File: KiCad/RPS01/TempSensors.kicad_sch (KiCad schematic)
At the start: 4 parts, among them J7 JST_PH_TEMP_SENSOR_1, J7 JST_PH_TEMP_SENSOR_2, J7 JST_PH_TEMP_SENSOR_3

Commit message: Large Schematic Update
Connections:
- net Temperature Data renamed VSIG
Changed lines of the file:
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@@
   (junction (at 139.1158 78.74) (diameter 0) (color 0 0 0 0)
   )
-  (junction (at 139.1158 78.8097) (diameter 0) (color 0 0 0 0)
+  (junction (at 146.7358 93.5482) (diameter 0) (color 0 0 0 0)
   )
-  (junction (at 146.7358 93.5482) (diameter 0) (color 0 0 0 0)
+  (junction (at 139.1158 79.502) (diameter 0) (color 0 0 0 0)
   )
   (junction (at 125.73 91.0082) (diameter 0) (color 0 0 0 0)
@@
   (junction (at 146.7358 106.7054) (diameter 0) (color 0 0 0 0)
   )
-  (wire (pts (xy 139.1158 78.8097) (xy 139.1158 91.0082))
+  (wire (pts (xy 125.73 91.0082) (xy 125.73 104.394))
     (stroke (width 0) (type default))
   )
-  (wire (pts (xy 125.73 91.0082) (xy 125.73 104.394))
+  (wire (pts (xy 125.73 90.17) (xy 125.73 91.0082))
     (stroke (width 0) (type default))
   )
@@
     (stroke (width 0) (type default))
   )
-  (wire (pts (xy 125.73 78.8097) (xy 125.73 90.17))
+  (wire (pts (xy 125.73 79.502) (xy 125.73 90.17))
     (stroke (width 0) (type default))
   )
@@
     (stroke (width 0) (type default))
   )
-  (wire (pts (xy 139.1158 78.8097) (xy 125.73 78.8097))
+  (wire (pts (xy 139.1158 79.502) (xy 125.73 79.502))
     (stroke (width 0) (type default))
   )
@@
     (stroke (width 0) (type default))
   )
-  (wire (pts (xy 125.73 90.17) (xy 125.73 91.0082))
-    (stroke (width 0) (type default))
-  )
   (wire (pts (xy 137.3886 75.7682) (xy 148.2598 75.7682))
     (stroke (width 0) (type default))
@@
     (stroke (width 0) (type default))
   )
-  (wire (pts (xy 125.73 78.74) (xy 139.1158 78.74))
+  (wire (pts (xy 139.1158 79.502) (xy 139.1158 91.0082))
     (stroke (width 0) (type default))
   )
@@
     (stroke (width 0) (type default))
   )
-  (wire (pts (xy 139.1158 78.74) (xy 139.1158 78.8097))
+  (wire (pts (xy 139.1158 78.74) (xy 139.1158 79.502))
     (stroke (width 0) (type default))
   )
@@
     (stroke (width 0) (type default))
   )
-  (hierarchical_label "Temperature Data" (shape input) (at 111.76 90.17 180) (fields_autoplaced)
+  (hierarchical_label "VSIG" (shape input) (at 111.76 90.17 180) (fields_autoplaced)
     (effects (font (size 1.27 1.27)) (justify right))
   )

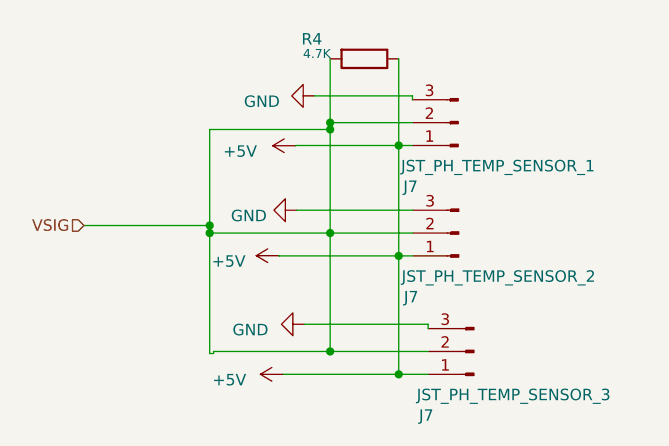
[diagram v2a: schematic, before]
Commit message: Finished most of the Schematics. Needs polishing
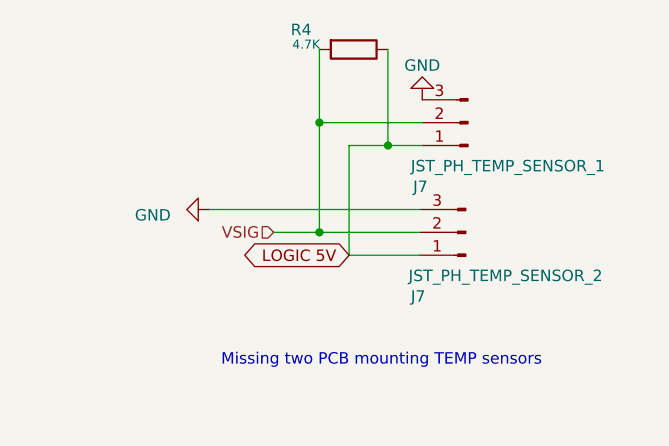
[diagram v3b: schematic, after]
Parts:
- removed J7: JST_PH_TEMP_SENSOR_3, Connector_JST:JST_PH_B3B-PH-K_1x03_P2.00mm_Vertical, symbol Connector:Conn_01x03_Pin
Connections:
- net +5V renamed LOGIC 5V
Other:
- note added: "Missing two PCB mounting TEMP sensors"
- moved on the sheet: J7, R4

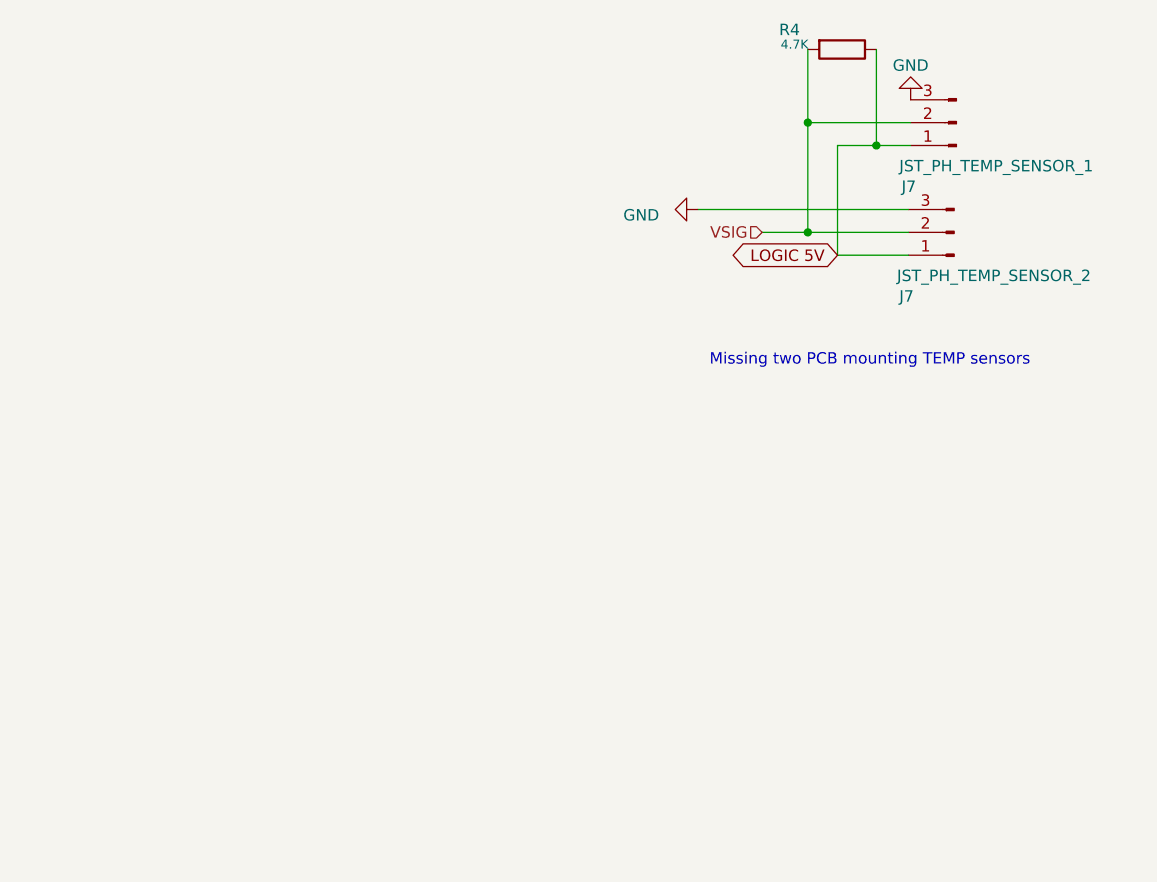
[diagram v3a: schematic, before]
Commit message: Finished Updating Footprints and Reorganized Reference Designators
Finished Updating Footprints and Reorganized Reference Designators

Starting to work on Final PCB, except for 19V Boost. Please check Schematic for errors
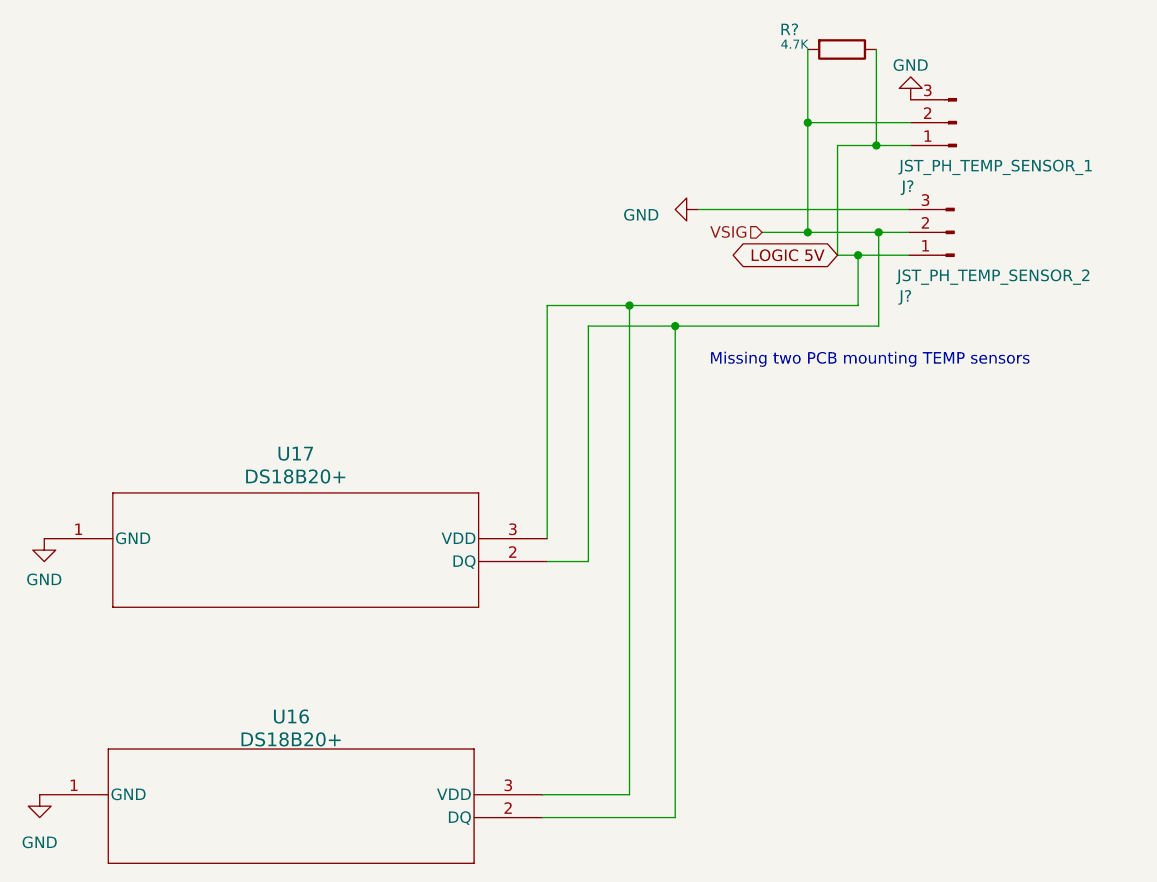
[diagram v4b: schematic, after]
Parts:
- added U16, U17: DS18B20+, Mechatronics TEMP:21-0248A_Q3-1_MXM, symbol Mechatronics TEMP:DS18B20+
- renumbered J7 to J?, R4 to R?
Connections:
- net GND: now also U16.1 (GND), U17.1 (GND)
- net LOGIC 5V: now also U16.3 (VDD), U17.3 (VDD)
- net VSIG: now also U16.2 (DQ), U17.2 (DQ)
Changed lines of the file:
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@@
 (kicad_sch (version 20230121) (generator eeschema)
   (paper "A4")
+  (junction (at 118.11 99.06) (diameter 0) (color 0 0 0 0)
+  )
   (junction (at 137.922 78.74) (diameter 0) (color 0 0 0 0)
   )
@@
   (junction (at 145.542 81.28) (diameter 0) (color 0 0 0 0)
   )
+  (junction (at 143.51 93.472) (diameter 0) (color 0 0 0 0)
+  )
+  (junction (at 145.796 90.932) (diameter 0) (color 0 0 0 0)
+  )
+  (junction (at 123.19 101.346) (diameter 0) (color 0 0 0 0)
+  )
   (wire (pts (xy 132.842 90.932) (xy 137.922 90.932))
     (stroke (width 0) (type default))
   )
+  (wire (pts (xy 143.51 99.06) (xy 143.51 93.472))
+    (stroke (width 0) (type default))
+  )
+  (wire (pts (xy 145.796 90.932) (xy 137.922 90.932))
+    (stroke (width 0) (type default))
+  )
+  (wire (pts (xy 108.966 127.508) (xy 113.538 127.508))
+    (stroke (width 0) (type default))
+  )
+  (wire (pts (xy 118.11 99.06) (xy 143.51 99.06))
+    (stroke (width 0) (type default))
+  )
+  (wire (pts (xy 108.458 153.416) (xy 118.11 153.416))
+    (stroke (width 0) (type default))
+  )
   (wire (pts (xy 141.224 81.28) (xy 141.224 93.472))
     (stroke (width 0) (type default))
   )
-  (wire (pts (xy 149.098 90.932) (xy 137.922 90.932))
+  (wire (pts (xy 149.098 90.932) (xy 145.796 90.932))
+    (stroke (width 0) (type default))
+  )
+  (wire (pts (xy 143.51 93.472) (xy 149.098 93.472))
     (stroke (width 0) (type default))
   )
@@
     (stroke (width 0) (type default))
   )
+  (wire (pts (xy 108.966 99.06) (xy 118.11 99.06))
+    (stroke (width 0) (type default))
+  )
+  (wire (pts (xy 113.538 101.346) (xy 123.19 101.346))
+    (stroke (width 0) (type default))
+  )
   (wire (pts (xy 137.922 70.612) (xy 137.922 78.74))
     (stroke (width 0) (type default))
   )
+  (wire (pts (xy 113.538 127.508) (xy 113.538 101.346))
+    (stroke (width 0) (type default))
+  )
+  (wire (pts (xy 118.11 153.416) (xy 118.11 99.06))
+    (stroke (width 0) (type default))
+  )
   (wire (pts (xy 137.922 78.74) (xy 149.352 78.74))
     (stroke (width 0) (type default))
@@
     (stroke (width 0) (type default))
   )
-  (wire (pts (xy 141.224 93.472) (xy 149.098 93.472))
+  (wire (pts (xy 141.224 93.472) (xy 143.51 93.472))
+    (stroke (width 0) (type default))
+  )
+  (wire (pts (xy 123.19 101.346) (xy 145.796 101.346))
     (stroke (width 0) (type default))
   )
@@
     (stroke (width 0) (type default))
   )
+  (wire (pts (xy 123.19 155.956) (xy 123.19 101.346))
+    (stroke (width 0) (type default))
+  )
+  (wire (pts (xy 108.966 124.968) (xy 108.966 99.06))
+    (stroke (width 0) (type default))
+  )
   (wire (pts (xy 145.542 81.28) (xy 149.352 81.28))
+    (stroke (width 0) (type default))
+  )
+  (wire (pts (xy 108.458 155.956) (xy 123.19 155.956))
+    (stroke (width 0) (type default))
+  )
+  (wire (pts (xy 145.796 101.346) (xy 145.796 90.932))
     (stroke (width 0) (type default))
   )
@@
   (symbol (lib_id "Device:R") (at 141.732 70.612 270) (unit 1)
     (in_bom yes) (on_board yes) (dnp no)
-    (property "Reference" "R4" (at 135.89 68.4276 90)
+    (property "Reference" "R?" (at 135.89 68.4276 90)
       (effects (font (size 1.27 1.27)))
     )
@@
       (project "MCU2"
         (path "/049009a7-95d1-4ccf-a10c-7859cfd6b188"
-          (reference "R4") (unit 1)
+          (reference "R?") (unit 1)
         )
       )
       (project "rps01"
         (path "/14930f15-c0a0-4b55-93e6-b112548415f6/a2e49fe6-126d-427d-b045-54fb7f662aa7"
-          (reference "R7") (unit 1)
+          (reference "R?") (unit 1)
         )
         (path "/14930f15-c0a0-4b55-93e6-b112548415f6"
-          (reference "R2") (unit 1)
-        )
-        (path "/14930f15-c0a0-4b55-93e6-b112548415f6/70788b2e-4f8b-415f-94db-6db5f6e45c82"
-          (reference "R19") (unit 1)
+          (reference "R?") (unit 1)
+        )
+        (path "/14930f15-c0a0-4b55-93e6-b112548415f6/70788b2e-4f8b-415f-94db-6db5f6e45c82"
+          (reference "R24") (unit 1)
         )
       )
       (project "M_MUC"
         (path "/8f0e16c9-4bd2-4a25-a569-54925ece9d23"
-          (reference "R1") (unit 1)
+          (reference "R?") (unit 1)
         )
       )
@@
   (symbol (lib_id "Connector:Conn_01x03_Pin") (at 154.178 90.932 180) (unit 1)
     (in_bom yes) (on_board yes) (dnp no)
-    (property "Reference" "J7" (at 148.082 98.044 0)
+    (property "Reference" "J?" (at 148.082 98.044 0)
       (effects (font (size 1.27 1.27)) (justify right))
     )
@@
       (project "rps01"
         (path "/14930f15-c0a0-4b55-93e6-b112548415f6/a2e49fe6-126d-427d-b045-54fb7f662aa7"
-          (reference "J7") (unit 1)
+          (reference "J?") (unit 1)
         )
         (path "/14930f15-c0a0-4b55-93e6-b112548415f6"
-          (reference "J11") (unit 1)
+          (reference "J?") (unit 1)
         )
         (path "/14930f15-c0a0-4b55-93e6-b112548415f6/70788b2e-4f8b-415f-94db-6db5f6e45c82"
@@
     )
   )
+  (symbol (lib_id "power:GND") (at 53.086 124.968 0) (unit 1)
+    (in_bom yes) (on_board yes) (dnp no) (fields_autoplaced)
+    (property "Reference" "#PWR044" (at 53.086 131.318 0)
+      (effects (font (size 1.27 1.27)) hide)
+    )
+    (property "Value" "GND" (at 53.086 129.54 0)
+      (effects (font (size 1.27 1.27)))
+    )
+    (property "Footprint" "" (at 53.086 124.968 0)
+      (effects (font (size 1.27 1.27)) hide)
+    )
+    (property "Datasheet" "" (at 53.086 124.968 0)
+      (effects (font (size 1.27 1.27)) hide)
+    )
+    (pin "1")
+    (instances
+      (project "rps01"
+        (path "/14930f15-c0a0-4b55-93e6-b112548415f6/70788b2e-4f8b-415f-94db-6db5f6e45c82"
+          (reference "#PWR044") (unit 1)
+        )
+      )
+    )
+  )
   (symbol (lib_id "power:GND") (at 149.352 76.2 180) (unit 1)
     (in_bom yes) (on_board yes) (dnp no) (fields_autoplaced)
-    (property "Reference" "#PWR044" (at 149.352 69.85 0)
+    (property "Reference" "#PWR046" (at 149.352 69.85 0)
       (effects (font (size 1.27 1.27)) hide)
     )
@@
       (project "rps01"
         (path "/14930f15-c0a0-4b55-93e6-b112548415f6/70788b2e-4f8b-415f-94db-6db5f6e45c82"
-          (reference "#PWR044") (unit 1)
+          (reference "#PWR046") (unit 1)
         )
       )
@@
   (symbol (lib_id "power:GND") (at 125.73 88.392 270) (unit 1)
     (in_bom yes) (on_board yes) (dnp no) (fields_autoplaced)
-    (property "Reference" "#PWR043" (at 119.38 88.392 0)
+    (property "Reference" "#PWR045" (at 119.38 88.392 0)
       (effects (font (size 1.27 1.27)) hide)
     )
@@
       (project "rps01"
         (path "/14930f15-c0a0-4b55-93e6-b112548415f6/70788b2e-4f8b-415f-94db-6db5f6e45c82"
+          (reference "#PWR045") (unit 1)
+        )
+      )
+    )
+  )
+  (symbol (lib_id "Mechatronics TEMP:DS18B20+") (at 52.578 153.416 0) (unit 1)
+    (in_bom yes) (on_board yes) (dnp no) (fields_autoplaced)
+    (property "Reference" "U16" (at 80.518 144.78 0)
+      (effects (font (size 1.524 1.524)))
+    )
+    (property "Value" "DS18B20+" (at 80.518 147.32 0)
+      (effects (font (size 1.524 1.524)))
+    )
+    (property "Footprint" "Mechatronics TEMP:21-0248A_Q3-1_MXM" (at 52.578 153.416 0)
+      (effects (font (size 1.27 1.27) italic) hide)
+    )
+    (property "Datasheet" "DS18B20+" (at 52.578 153.416 0)
+      (effects (font (size 1.27 1.27) italic) hide)
+    )
+    (pin "1")
+    (pin "2")
+    (pin "3")
+    (instances
+      (project "rps01"
+        (path "/14930f15-c0a0-4b55-93e6-b112548415f6/70788b2e-4f8b-415f-94db-6db5f6e45c82"
+          (reference "U16") (unit 1)
+        )
+      )
+    )
+  )
+  (symbol (lib_id "power:GND") (at 52.578 153.416 0) (unit 1)
+    (in_bom yes) (on_board yes) (dnp no) (fields_autoplaced)
+    (property "Reference" "#PWR043" (at 52.578 159.766 0)
+      (effects (font (size 1.27 1.27)) hide)
+    )
+    (property "Value" "GND" (at 52.578 158.75 0)
+      (effects (font (size 1.27 1.27)))
+    )
+    (property "Footprint" "" (at 52.578 153.416 0)
+      (effects (font (size 1.27 1.27)) hide)
+    )
+    (property "Datasheet" "" (at 52.578 153.416 0)
+      (effects (font (size 1.27 1.27)) hide)
+    )
+    (pin "1")
+    (instances
+      (project "rps01"
+        (path "/14930f15-c0a0-4b55-93e6-b112548415f6/70788b2e-4f8b-415f-94db-6db5f6e45c82"
           (reference "#PWR043") (unit 1)
+        )
+      )
+    )
+  )
+  (symbol (lib_id "Mechatronics TEMP:DS18B20+") (at 53.086 124.968 0) (unit 1)
+    (in_bom yes) (on_board yes) (dnp no) (fields_autoplaced)
+    (property "Reference" "U17" (at 81.026 115.57 0)
+      (effects (font (size 1.524 1.524)))
+    )
+    (property "Value" "DS18B20+" (at 81.026 118.11 0)
+      (effects (font (size 1.524 1.524)))
+    )
+    (property "Footprint" "Mechatronics TEMP:21-0248A_Q3-1_MXM" (at 53.086 124.968 0)
+      (effects (font (size 1.27 1.27) italic) hide)
+    )
+    (property "Datasheet" "DS18B20+" (at 53.086 124.968 0)
+      (effects (font (size 1.27 1.27) italic) hide)
+    )
+    (pin "1")
+    (pin "2")
+    (pin "3")
+    (instances
+      (project "rps01"
+        (path "/14930f15-c0a0-4b55-93e6-b112548415f6/70788b2e-4f8b-415f-94db-6db5f6e45c82"
+          (reference "U17") (unit 1)
         )
       )
@@
   (symbol (lib_id "Connector:Conn_01x03_Pin") (at 154.432 78.74 180) (unit 1)
     (in_bom yes) (on_board yes) (dnp no)
-    (property "Reference" "J7" (at 148.336 85.852 0)
+    (property "Reference" "J?" (at 148.336 85.852 0)
       (effects (font (size 1.27 1.27)) (justify right))
     )
@@
       (project "rps01"
         (path "/14930f15-c0a0-4b55-93e6-b112548415f6/a2e49fe6-126d-427d-b045-54fb7f662aa7"
-          (reference "J7") (unit 1)
+          (reference "J?") (unit 1)
         )
         (path "/14930f15-c0a0-4b55-93e6-b112548415f6"
-          (reference "J7") (unit 1)
-        )
-        (path "/14930f15-c0a0-4b55-93e6-b112548415f6/70788b2e-4f8b-415f-94db-6db5f6e45c82"
+          (reference "J?") (unit 1)
+        )
+        (path "/14930f15-c0a0-4b55-93e6-b112548415f6/70788b2e-4f8b-415f-94db-6db5f6e45c82"

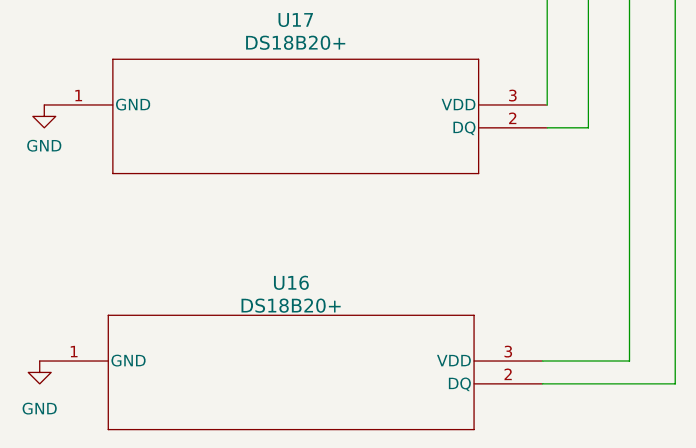
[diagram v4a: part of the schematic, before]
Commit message: Board Ready For layout. Except for 19V Boost? CHECK vs SIM Please
Board Ready For layout. Except for 19V Boost? CHECK vs SIM Please
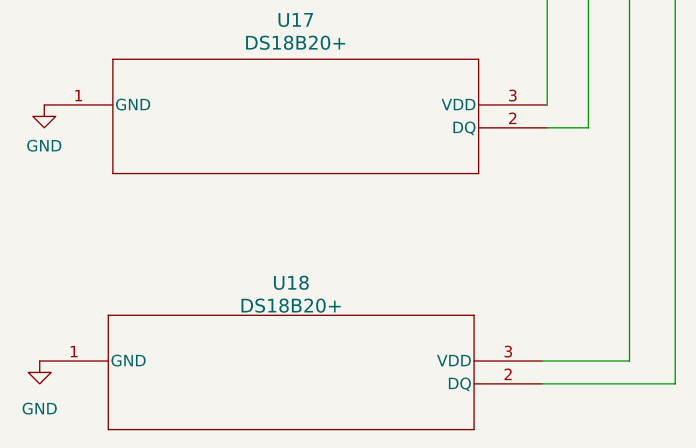
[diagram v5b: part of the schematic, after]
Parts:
- renumbered U16 to U18
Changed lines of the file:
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@@
         )
         (path "/14930f15-c0a0-4b55-93e6-b112548415f6/70788b2e-4f8b-415f-94db-6db5f6e45c82"
-          (reference "R24") (unit 1)
+          (reference "R27") (unit 1)
         )
       )
@@
         )
         (path "/14930f15-c0a0-4b55-93e6-b112548415f6/70788b2e-4f8b-415f-94db-6db5f6e45c82"
-          (reference "J12") (unit 1)
+          (reference "J14") (unit 1)
         )
       )
@@
   (symbol (lib_id "power:GND") (at 53.086 124.968 0) (unit 1)
     (in_bom yes) (on_board yes) (dnp no) (fields_autoplaced)
-    (property "Reference" "#PWR044" (at 53.086 131.318 0)
+    (property "Reference" "#PWR070" (at 53.086 131.318 0)
       (effects (font (size 1.27 1.27)) hide)
     )
@@
       (project "rps01"
         (path "/14930f15-c0a0-4b55-93e6-b112548415f6/70788b2e-4f8b-415f-94db-6db5f6e45c82"
-          (reference "#PWR044") (unit 1)
+          (reference "#PWR070") (unit 1)
         )
       )
@@
   (symbol (lib_id "power:GND") (at 149.352 76.2 180) (unit 1)
     (in_bom yes) (on_board yes) (dnp no) (fields_autoplaced)
-    (property "Reference" "#PWR046" (at 149.352 69.85 0)
+    (property "Reference" "#PWR068" (at 149.352 69.85 0)
       (effects (font (size 1.27 1.27)) hide)
     )
@@
       (project "rps01"
         (path "/14930f15-c0a0-4b55-93e6-b112548415f6/70788b2e-4f8b-415f-94db-6db5f6e45c82"
-          (reference "#PWR046") (unit 1)
+          (reference "#PWR068") (unit 1)
         )
       )
@@
   (symbol (lib_id "power:GND") (at 125.73 88.392 270) (unit 1)
     (in_bom yes) (on_board yes) (dnp no) (fields_autoplaced)
-    (property "Reference" "#PWR045" (at 119.38 88.392 0)
+    (property "Reference" "#PWR069" (at 119.38 88.392 0)
       (effects (font (size 1.27 1.27)) hide)
     )
@@
       (project "rps01"
         (path "/14930f15-c0a0-4b55-93e6-b112548415f6/70788b2e-4f8b-415f-94db-6db5f6e45c82"
-          (reference "#PWR045") (unit 1)
+          (reference "#PWR069") (unit 1)
         )
       )
@@
   (symbol (lib_id "Mechatronics TEMP:DS18B20+") (at 52.578 153.416 0) (unit 1)
     (in_bom yes) (on_board yes) (dnp no) (fields_autoplaced)
-    (property "Reference" "U16" (at 80.518 144.78 0)
+    (property "Reference" "U18" (at 80.518 144.78 0)
       (effects (font (size 1.524 1.524)))
     )
@@
       (project "rps01"
         (path "/14930f15-c0a0-4b55-93e6-b112548415f6/70788b2e-4f8b-415f-94db-6db5f6e45c82"
-          (reference "U16") (unit 1)
+          (reference "U18") (unit 1)
         )
       )
@@
   (symbol (lib_id "power:GND") (at 52.578 153.416 0) (unit 1)
     (in_bom yes) (on_board yes) (dnp no) (fields_autoplaced)
-    (property "Reference" "#PWR043" (at 52.578 159.766 0)
+    (property "Reference" "#PWR071" (at 52.578 159.766 0)
       (effects (font (size 1.27 1.27)) hide)
     )
@@
       (project "rps01"
         (path "/14930f15-c0a0-4b55-93e6-b112548415f6/70788b2e-4f8b-415f-94db-6db5f6e45c82"
-          (reference "#PWR043") (unit 1)
+          (reference "#PWR071") (unit 1)
         )
       )
